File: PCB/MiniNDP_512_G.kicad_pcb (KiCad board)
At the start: 2 copper layers, 60 x 34 mm, 19 parts, among them J1 Conn_02x20_Odd_Even, U1 HC238, U2 HC4040, U3 FCT841, U4 AS6C4008, U5 HC00

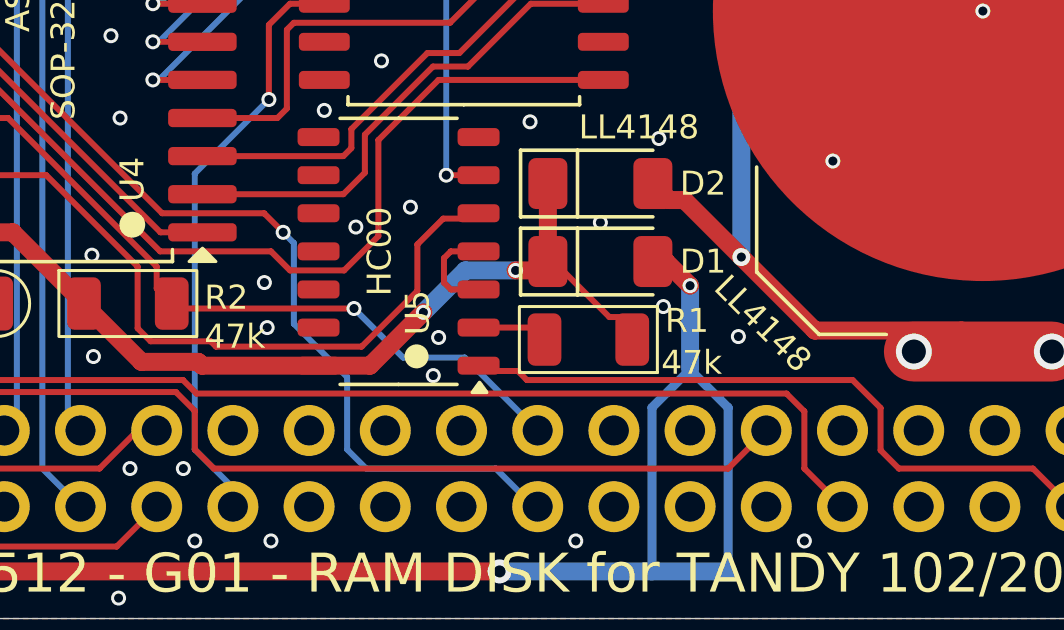
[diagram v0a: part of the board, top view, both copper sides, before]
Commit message: 512_G missing trace ramrst to nand
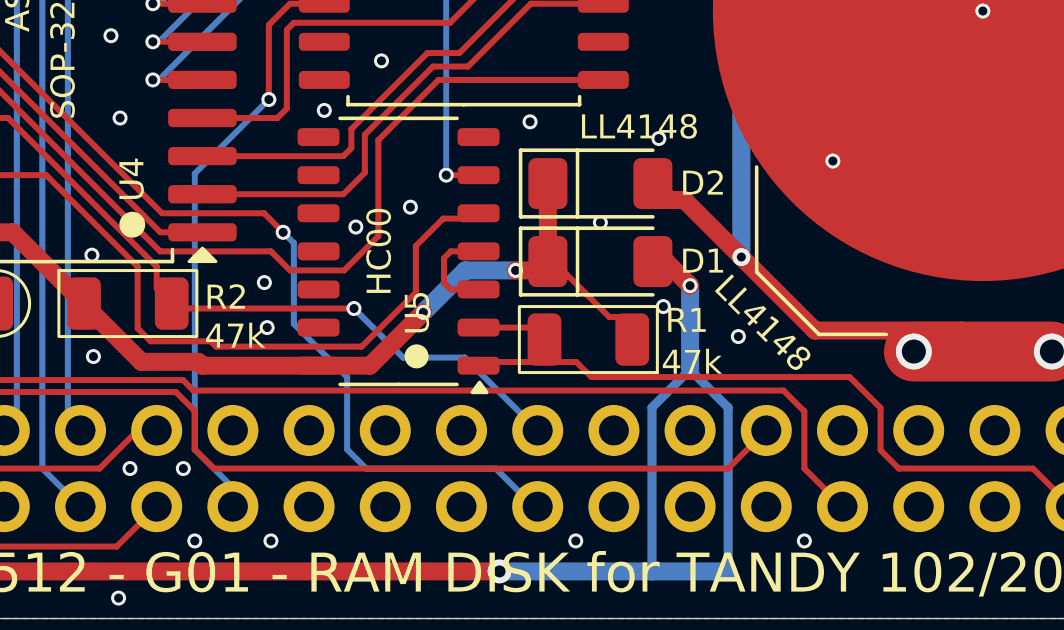
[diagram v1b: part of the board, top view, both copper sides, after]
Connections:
- R1 pad 2: Net-(R1-Pad2) -> /RAMRST
- U5 pad 2: Net-(R1-Pad2) -> /RAMRST
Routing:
- net /RAMRST: track 22.5 -> 25.7 mm
- net Net-(R1-Pad2): track 2.36 -> 0.00 mm
- net GND: vias 68 -> 66
